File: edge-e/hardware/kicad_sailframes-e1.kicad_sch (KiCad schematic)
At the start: 6 parts, among them J1 Conn_01x06, J2 Conn_01x04, J3 Conn_01x10, J4 Conn_01x04, J5 Conn_01x02

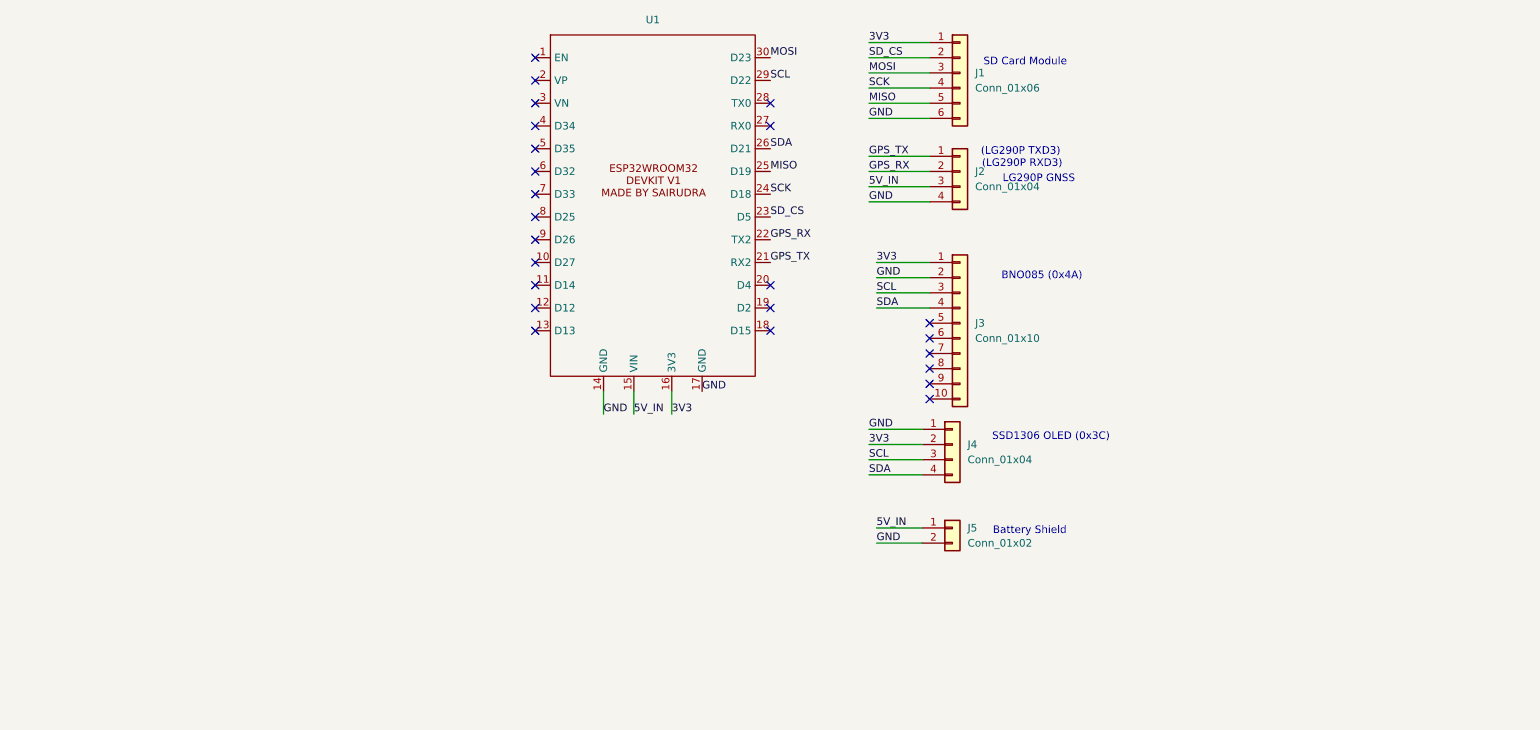
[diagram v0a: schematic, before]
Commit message: E1 PCB v1.0: complete KiCad design with TFT display
Hardware changes:
- Replace OLED with Hosyond 3.5 TFT ST7796U for sunlight readability
- TFT on VSPI bus, SD card on HSPI bus - eliminates display flicker
- Replace PowerBoost 1000C with DWEII USB-C boost charger
- Add 6000mAh LiPo battery with JST PH 2.0mm connector
- Battery voltage divider: 2x 100K for ADC monitoring

PCB design:
- 60.5 x 91.5mm, 2-layer board
- Connectors: GPS, IMU, TFT, SD, battery, power switch
- Expansion: Wind sensor UART1, I2C headers, GPIO expansion
- Ground pour on bottom layer
- Gerbers generated and ordered from JLCPCB

Pin swaps in User_Setup.h to match soldered prototype:
- TFT_MISO: GPIO19 to GPIO25
- TFT_BL: GPIO25 to GPIO19

Co-Authored-By: Claude Opus 4.5 <noreply@anthropic.com>
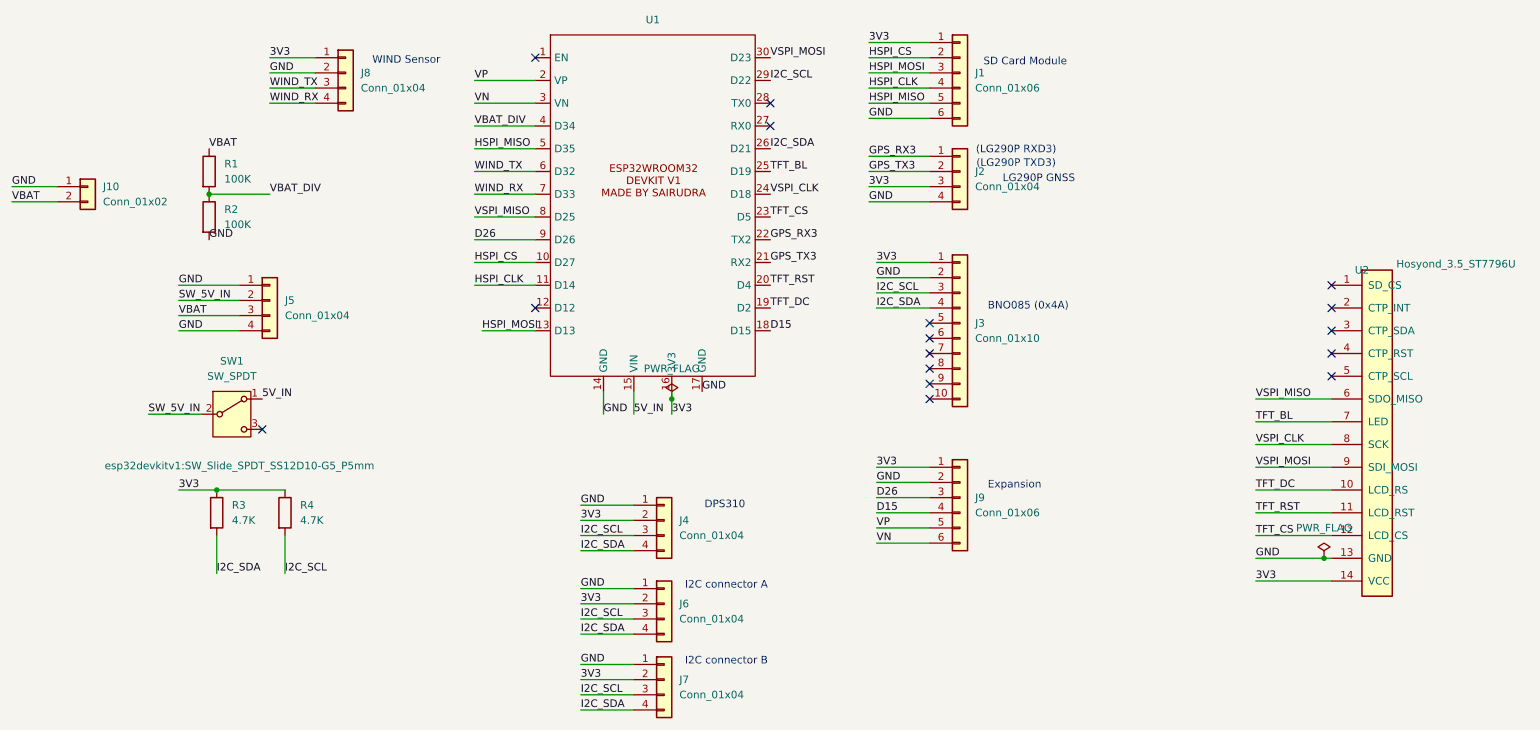
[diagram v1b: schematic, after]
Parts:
- removed J5: Conn_01x02, Connector_PinHeader_2.54mm:PinHeader_1x02_P2.54mm_Vertical, symbol Connector_Generic:Conn_01x02
- added J10: Conn_01x02, Connector_JST:JST_PH_S2B-PH-K_1x02_P2.00mm_Horizontal, symbol Connector_Generic:Conn_01x02
- added J5, J6, J7, J8: Conn_01x04, Connector_PinHeader_2.54mm:PinHeader_1x04_P2.54mm_Vertical, symbol Connector_Generic:Conn_01x04
- added J9: Conn_01x06, Connector_PinHeader_2.54mm:PinHeader_1x06_P2.54mm_Vertical, symbol Connector_Generic:Conn_01x06
- added R1, R2: 100K, Resistor_SMD:R_0805_2012Metric, symbol Device:R
- added R3, R4: 4.7K, Resistor_SMD:R_0805_2012Metric, symbol Device:R
- added SW1: SW_SPDT, esp32devkitv1:SW_Slide_SPDT_SS12D10-G5_P5mm, symbol Switch:SW_SPDT
- added U2: Hosyond_3.5_ST7796U, Connector_PinHeader_2.54mm:PinHeader_1x14_P2.54mm_Vertical, symbol Hosyond:Hosyond_3.5_ST7796U
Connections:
- net 3V3: now also J2.3 (Pin_3), J6.2 (Pin_2), J7.2 (Pin_2), J8.1 (Pin_1), J9.1 (Pin_1), R3.1, R4.1, U2.14 (VCC)
- net 5V_IN: now also SW1.1 (A); no longer J2.3 (Pin_3)
- net GND: now also J10.1 (Pin_1), J5.1 (Pin_1), J5.4 (Pin_4), J6.1 (Pin_1), J7.1 (Pin_1), J8.2 (Pin_2), J9.2 (Pin_2), R2.2, U2.13 (GND)
- net HSPI_CS: now reaches U1.10 (D27)
- net HSPI_CS: now also J1.2 (Pin_2)
- net HSPI_CLK: now reaches U1.11 (D14)
- net HSPI_CLK: now also J1.4 (Pin_4)
- net HSPI_MOSI: now reaches U1.13 (D13)
- net HSPI_MOSI: now also J1.3 (Pin_3)
- net D15: now reaches U1.18 (D15)
- net D15: now also J9.4 (Pin_4)
- net TFT_DC: now reaches U1.19 (D2)
- net TFT_DC: now also U2.10 (LCD_RS)
- net VP: now reaches U1.2 (VP)
- net VP: now also J9.5 (Pin_5)
- net TFT_RST: now reaches U1.20 (D4)
- net TFT_RST: now also U2.11 (LCD_RST)
- net VN: now reaches U1.3 (VN)
- net VN: now also J9.6 (Pin_6)
- net VBAT_DIV: now reaches U1.4 (D34)
- net VBAT_DIV: now also R1.2, R2.1
- net HSPI_MISO: now reaches U1.5 (D35)
- net HSPI_MISO: now also J1.5 (Pin_5)
- net WIND_TX: now reaches U1.6 (D32)
- net WIND_TX: now also J8.3 (Pin_3)
- net WIND_RX: now reaches U1.7 (D33)
- net WIND_RX: now also J8.4 (Pin_4)
- net VSPI_MISO: now reaches U1.8 (D25)
- net VSPI_MISO: now also U2.6 (SDO_MISO)
- net D26: now reaches U1.9 (D26)
- net D26: now also J9.3 (Pin_3)
- net GPS_RX renamed GPS_RX3
- net GPS_RX3: now also J2.1 (Pin_1); no longer J2.2 (Pin_2)
- net GPS_TX renamed GPS_TX3
- net GPS_TX3: now also J2.2 (Pin_2); no longer J2.1 (Pin_1)
- net MISO renamed TFT_BL
- net TFT_BL: now also U2.7 (LED); no longer J1.5 (Pin_5)
- net MOSI renamed VSPI_MOSI
- net VSPI_MOSI: now also U2.9 (SDI_MOSI); no longer J1.3 (Pin_3)
- net SCK renamed VSPI_CLK
- net VSPI_CLK: now also U2.8 (SCK); no longer J1.4 (Pin_4)
- net SCL renamed I2C_SCL
- net I2C_SCL: now also J6.3 (Pin_3), J7.3 (Pin_3), R4.2
- net SDA renamed I2C_SDA
- net I2C_SDA: now also J6.4 (Pin_4), J7.4 (Pin_4), R3.2
- net SD_CS renamed TFT_CS
- net TFT_CS: now also U2.12 (LCD_CS); no longer J1.2 (Pin_2)
- new net SW_5V_IN: J5.2 (Pin_2), SW1.2 (B)
- new net VBAT: J10.2 (Pin_2), J5.3 (Pin_3), R1.1
- no-connect marks 24 -> 16
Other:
- note added: "DPS310"
- note added: "Expansion"
- note added: "I2C connector A"
- note added: "I2C connector B"
- note added: "WIND Sensor"
- note removed: "Battery Shield"
- note removed: "SSD1306 OLED (0x3C)"
- moved on the sheet: J4

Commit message: E1 PCB v1.1: add ground pour, mounting holes, and layout updates
Hardware:
- Add ground pour on B.Cu layer for improved EMI shielding
- Add 4x M2.5 mounting holes at corners
- Update PCB layout with component repositioning
- Add custom SPDT switch footprint (SS12D10-G5)
- Remove unused footprint libraries (DWEII, esp32devkitv1)
- Add BOM, Gerber job file, and Specctra DSN export

Firmware:
- Add E1 SD card config files (config.txt, imu_cal.txt, wind_mac.txt)

Web dashboard:
- Update chart panel and map view components
- CSS and layout improvements

Lambda/Scripts:
- Update PPK processing and upload handlers
- Add GPS reprocessing scripts (10Hz, timestamps, all sessions)
- Add session restore utility

Documentation:
- Add E1 display upgrade, firmware MSM, and power/battery specs
- Update LG290P configuration notes
- Add RTKLIB obs codes fix documentation

Co-Authored-By: Claude Opus 4.5 <noreply@anthropic.com>
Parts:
- SW1: footprint esp32devkitv1:SW_Slide_SPDT_SS12D10-G5_P5mm -> e1_Library:SW_Slide_SS12D10-G5_v3_SAILFRAMES
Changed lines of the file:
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@@
 			)
 		)
-		(property "Footprint" "esp32devkitv1:SW_Slide_SPDT_SS12D10-G5_P5mm"
+		(property "Footprint" "e1_Library:SW_Slide_SS12D10-G5_v3_SAILFRAMES"
 			(at 67.31 139.446 0)
 			(show_name no)
